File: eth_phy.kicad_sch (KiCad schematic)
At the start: 33 parts, among them J4 RJ45_Hanrun_HR911105A_Horizon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, U2 LAN8742A

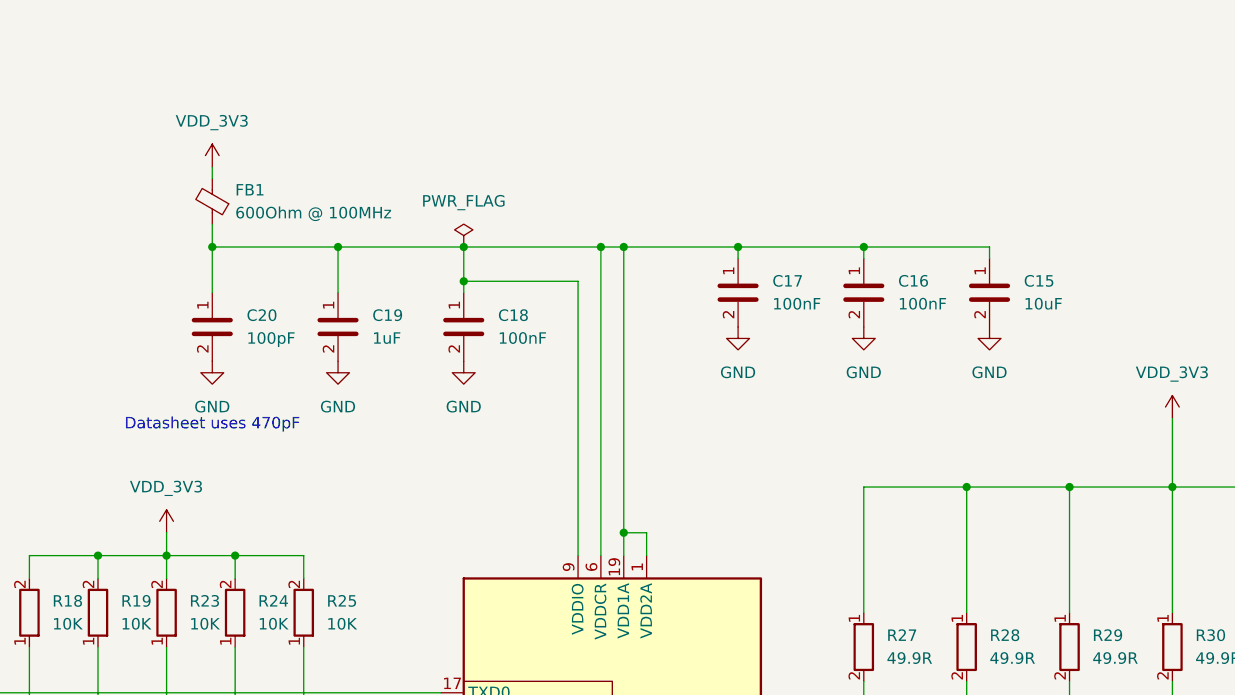
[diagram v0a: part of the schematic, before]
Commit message: fix: removed 3v3 on 1.2v lan core voltage
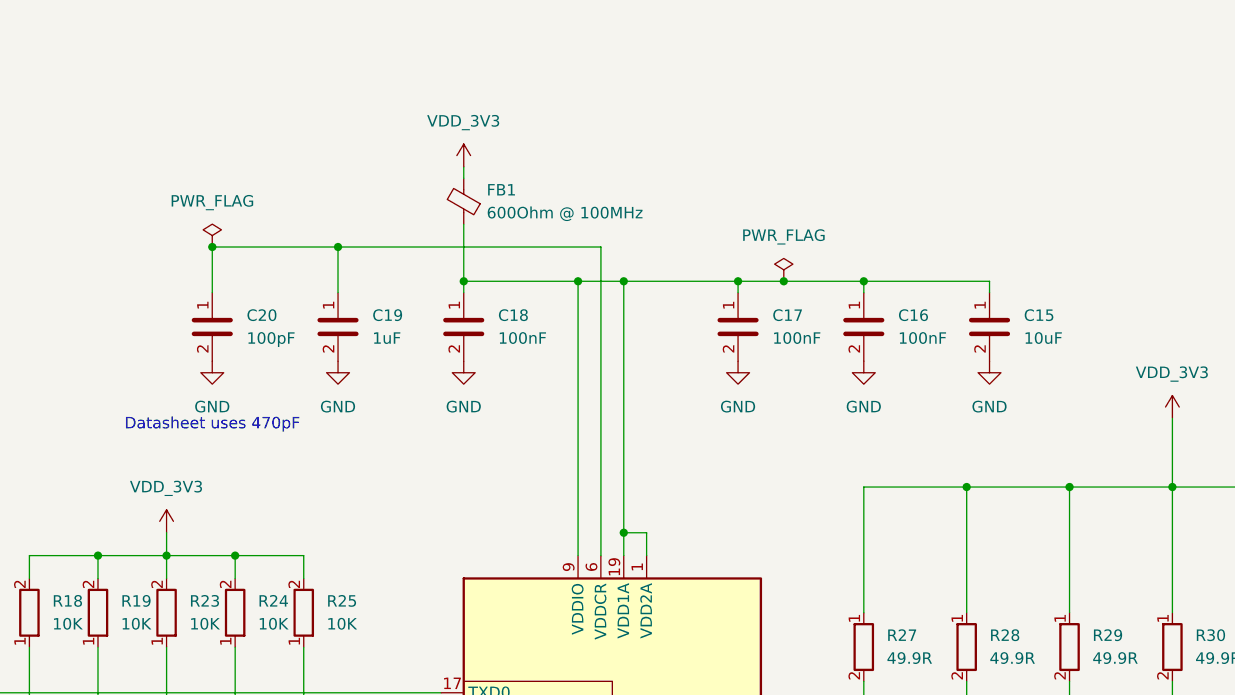
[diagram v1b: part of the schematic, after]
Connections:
- net at C15.1, C16.1, C17.1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: no longer C19.1, C20.1, U2.6 (VDDCR)
- new net: C19.1, C20.1, U2.6 (VDDCR)
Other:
- moved on the sheet: C15, C16, C17, FB1
